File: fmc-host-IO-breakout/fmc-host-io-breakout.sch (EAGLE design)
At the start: 79 parts, among them J4 12226-8250-00FR, X1 1503_02

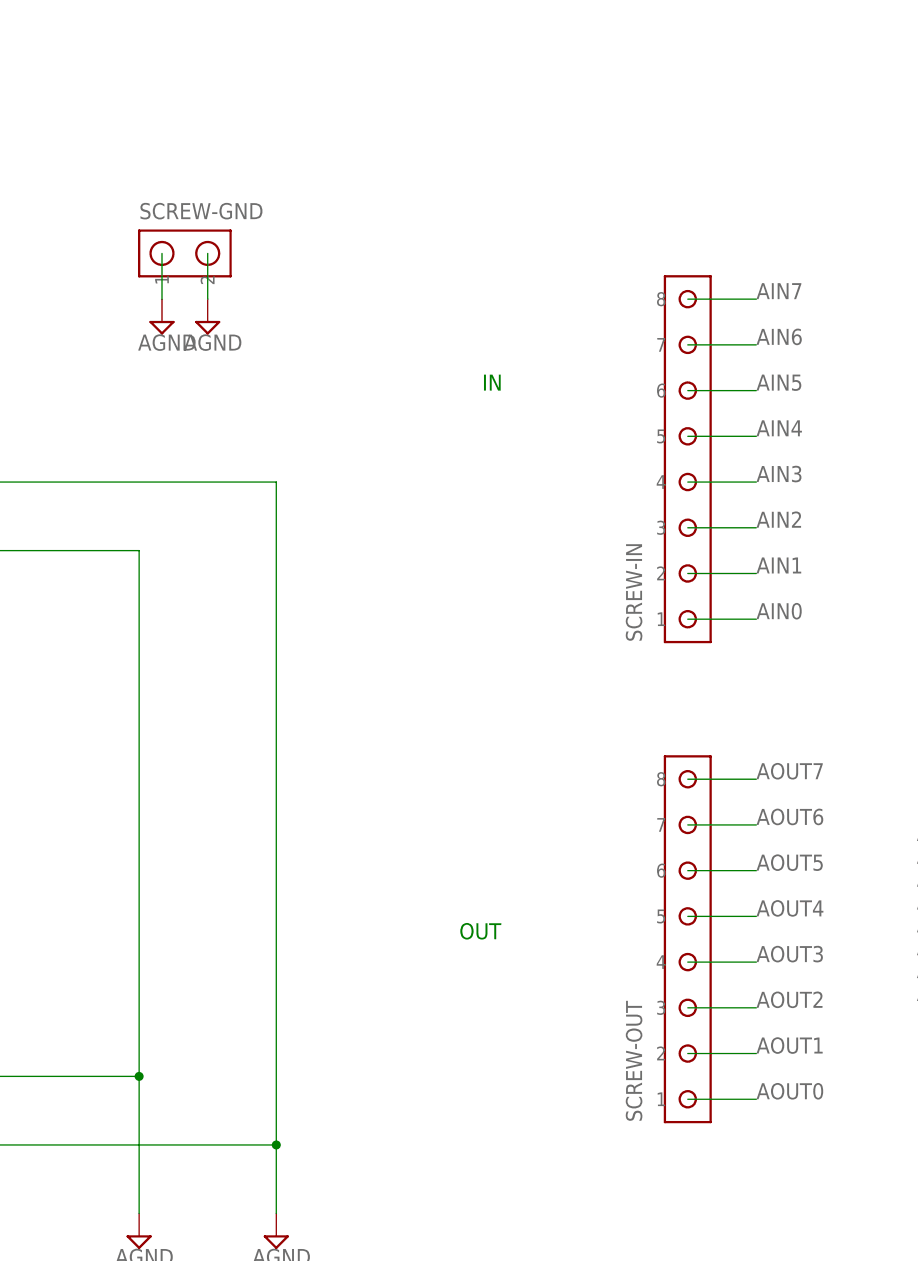
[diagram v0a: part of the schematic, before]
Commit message: Made analog io board compatible with screwless screw terminals
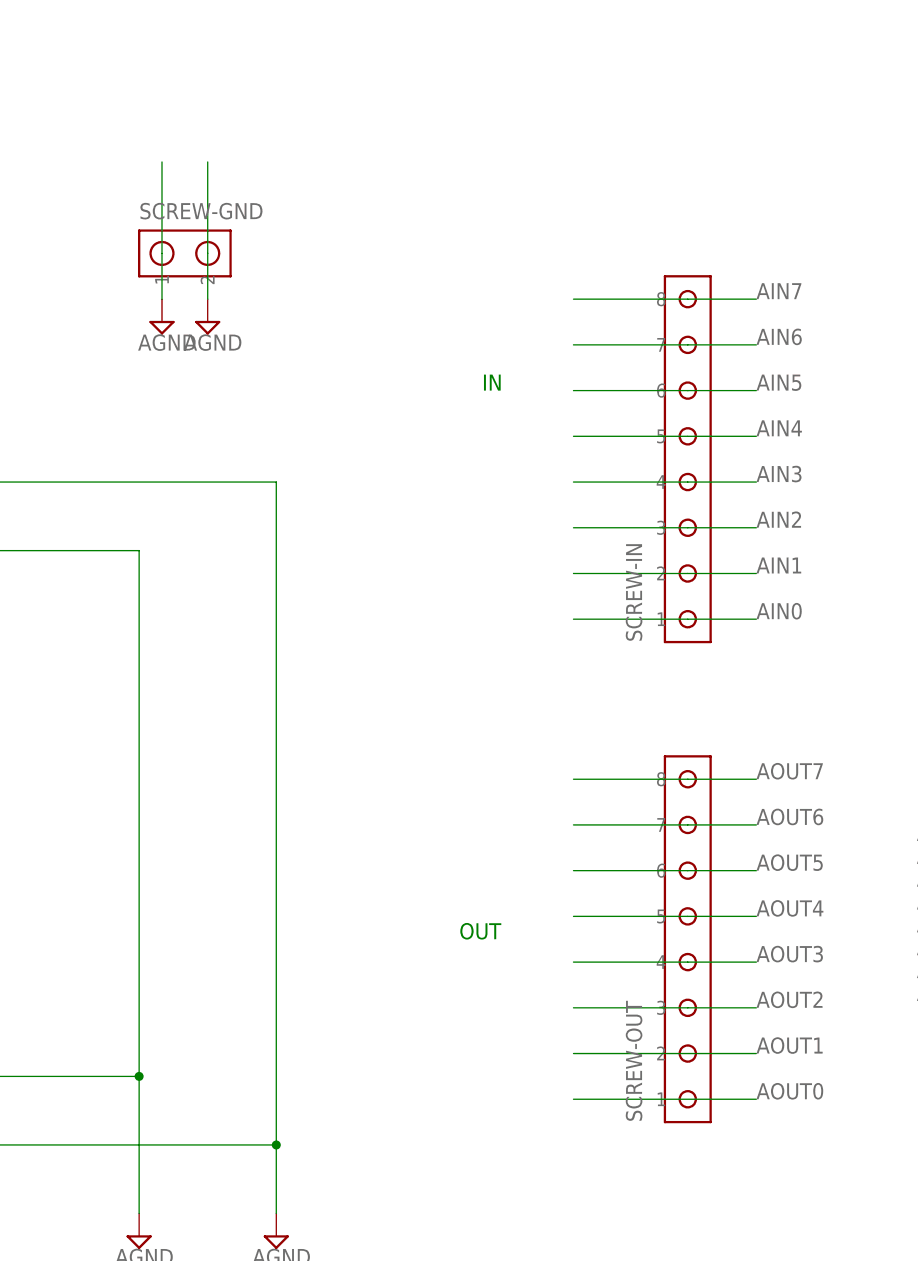
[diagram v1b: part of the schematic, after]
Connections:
- net AOUT0: no longer SCREW-OUT.1
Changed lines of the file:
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@@
 <pinref part="SUPPLY9" gate="G$1" pin="AGND"/>
 <wire x1="58.42" y1="167.64" x2="58.42" y2="162.56" width="0.1524" layer="91"/>
+<wire x1="58.42" y1="177.8" x2="58.42" y2="167.64" width="0.1524" layer="91"/>
 </segment>
 <segment>
@@
 <pinref part="SUPPLY10" gate="G$1" pin="AGND"/>
 <wire x1="63.5" y1="167.64" x2="63.5" y2="162.56" width="0.1524" layer="91"/>
+<wire x1="63.5" y1="177.8" x2="63.5" y2="167.64" width="0.1524" layer="91"/>
 </segment>
 <segment>
@@
 <wire x1="116.84" y1="127" x2="124.46" y2="127" width="0.1524" layer="91"/>
 <label x="124.46" y="127" size="1.778" layer="95"/>
+<wire x1="104.14" y1="127" x2="116.84" y2="127" width="0.1524" layer="91"/>
 </segment>
 <segment>
@@
 <wire x1="116.84" y1="132.08" x2="124.46" y2="132.08" width="0.1524" layer="91"/>
 <label x="124.46" y="132.08" size="1.778" layer="95"/>
+<wire x1="104.14" y1="132.08" x2="116.84" y2="132.08" width="0.1524" layer="91"/>
 </segment>
 <segment>
@@
 <wire x1="116.84" y1="137.16" x2="124.46" y2="137.16" width="0.1524" layer="91"/>
 <label x="124.46" y="137.16" size="1.778" layer="95"/>
+<wire x1="104.14" y1="137.16" x2="116.84" y2="137.16" width="0.1524" layer="91"/>
 </segment>
 <segment>
@@
 <wire x1="116.84" y1="142.24" x2="124.46" y2="142.24" width="0.1524" layer="91"/>
 <label x="124.46" y="142.24" size="1.778" layer="95"/>
+<wire x1="104.14" y1="142.24" x2="116.84" y2="142.24" width="0.1524" layer="91"/>
 </segment>
 <segment>
@@
 <wire x1="116.84" y1="147.32" x2="124.46" y2="147.32" width="0.1524" layer="91"/>
 <label x="124.46" y="147.32" size="1.778" layer="95"/>
+<wire x1="104.14" y1="147.32" x2="116.84" y2="147.32" width="0.1524" layer="91"/>
 </segment>
 <segment>
@@
 <wire x1="116.84" y1="152.4" x2="124.46" y2="152.4" width="0.1524" layer="91"/>
 <label x="124.46" y="152.4" size="1.778" layer="95"/>
+<wire x1="104.14" y1="152.4" x2="116.84" y2="152.4" width="0.1524" layer="91"/>
 </segment>
 <segment>
@@
 <wire x1="116.84" y1="157.48" x2="124.46" y2="157.48" width="0.1524" layer="91"/>
 <label x="124.46" y="157.48" size="1.778" layer="95"/>
+<wire x1="104.14" y1="157.48" x2="116.84" y2="157.48" width="0.1524" layer="91"/>
 </segment>
 <segment>
@@
 <wire x1="116.84" y1="162.56" x2="124.46" y2="162.56" width="0.1524" layer="91"/>
 <label x="124.46" y="162.56" size="1.778" layer="95"/>
+<wire x1="104.14" y1="162.56" x2="116.84" y2="162.56" width="0.1524" layer="91"/>
 </segment>
 <segment>
@@
 <wire x1="116.84" y1="78.74" x2="124.46" y2="78.74" width="0.1524" layer="91"/>
 <label x="124.46" y="78.74" size="1.778" layer="95"/>
+<wire x1="104.14" y1="78.74" x2="116.84" y2="78.74" width="0.1524" layer="91"/>
 </segment>
 <segment>
@@
 <wire x1="116.84" y1="83.82" x2="124.46" y2="83.82" width="0.1524" layer="91"/>
 <label x="124.46" y="83.82" size="1.778" layer="95"/>
+<wire x1="104.14" y1="83.82" x2="116.84" y2="83.82" width="0.1524" layer="91"/>
 </segment>
 <segment>
@@
 <wire x1="116.84" y1="93.98" x2="124.46" y2="93.98" width="0.1524" layer="91"/>
 <label x="124.46" y="93.98" size="1.778" layer="95"/>
+<wire x1="104.14" y1="93.98" x2="116.84" y2="93.98" width="0.1524" layer="91"/>
 </segment>
 <segment>
@@
 <wire x1="116.84" y1="99.06" x2="124.46" y2="99.06" width="0.1524" layer="91"/>
 <label x="124.46" y="99.06" size="1.778" layer="95"/>
+<wire x1="104.14" y1="99.06" x2="116.84" y2="99.06" width="0.1524" layer="91"/>
 </segment>
 <segment>
@@
 <wire x1="116.84" y1="104.14" x2="124.46" y2="104.14" width="0.1524" layer="91"/>
 <label x="124.46" y="104.14" size="1.778" layer="95"/>
+<wire x1="104.14" y1="104.14" x2="116.84" y2="104.14" width="0.1524" layer="91"/>
 </segment>
 <segment>
@@
 <wire x1="116.84" y1="88.9" x2="124.46" y2="88.9" width="0.1524" layer="91"/>
 <label x="124.46" y="88.9" size="1.778" layer="95"/>
+<wire x1="104.14" y1="88.9" x2="116.84" y2="88.9" width="0.1524" layer="91"/>
 </segment>
 <segment>
@@
 </segment>
 <segment>
-<pinref part="SCREW-OUT" gate="G$1" pin="1"/>
-<wire x1="124.46" y1="73.66" x2="116.84" y2="73.66" width="0.1524" layer="91"/>
+<wire x1="124.46" y1="73.66" x2="104.14" y2="73.66" width="0.1524" layer="91"/>
 <label x="124.46" y="73.66" size="1.778" layer="95"/>
 </segment>
@@
 <wire x1="116.84" y1="109.22" x2="124.46" y2="109.22" width="0.1524" layer="91"/>
 <label x="124.46" y="109.22" size="1.778" layer="95"/>
-</segment>
-<segment>
+<wire x1="104.14" y1="109.22" x2="116.84" y2="109.22" width="0.1524" layer="91"/>
+</segment>
+<segment>

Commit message: Connected screw terminal rows in analog io board
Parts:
- added SCREW-GND2: SCREW2, jonnew:SCREW2
- added SCREW-OUT1, SCREW-OUT2: SCREW8, jonnew:SCREW8
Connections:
- net AGND: now also SCREW-GND2.1, SCREW-GND2.2
- net AIN0: now also SCREW-OUT1.1
- net AIN1: now also SCREW-OUT1.2
- net AIN2: now also SCREW-OUT1.3
- net AIN3: now also SCREW-OUT1.4
- net AIN4: now also SCREW-OUT1.5
- net AIN5: now also SCREW-OUT1.6
- net AIN6: now also SCREW-OUT1.7
- net AIN7: now also SCREW-OUT1.8
- net AOUT0: now also SCREW-OUT.1, SCREW-OUT2.1
- net AOUT1: now also SCREW-OUT2.2
- net AOUT2: now also SCREW-OUT2.3
- net AOUT3: now also SCREW-OUT2.4
- net AOUT4: now also SCREW-OUT2.5
- net AOUT5: now also SCREW-OUT2.6
- net AOUT6: now also SCREW-OUT2.7
- net AOUT7: now also SCREW-OUT2.8
